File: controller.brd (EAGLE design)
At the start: 100 x 100 mm, 38 parts, among them IC1 7805DT, Q2 MOSFET-NCHANNELBSS123LT1G, Q3 MOSFET-NCHANNELFDD8780, U1 ATMEGA328P, Y1 16MHz

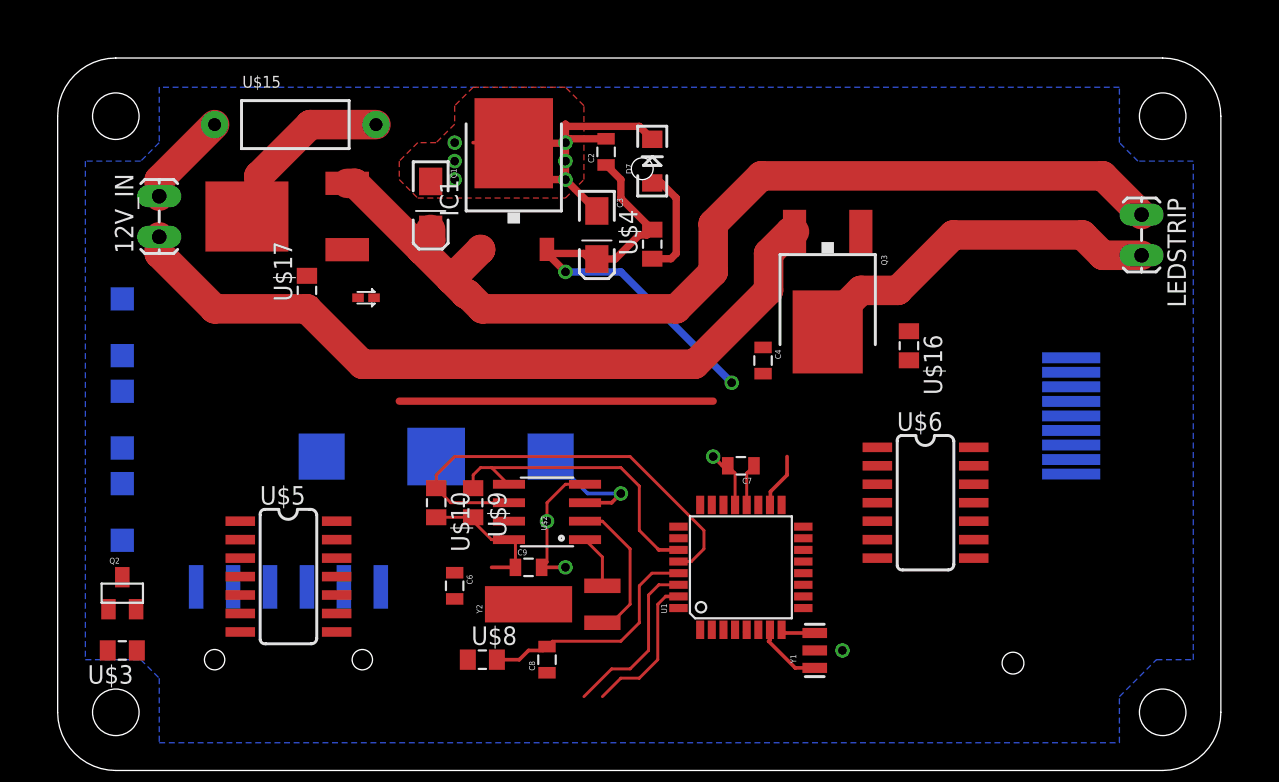
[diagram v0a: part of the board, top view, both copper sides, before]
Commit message: added sense IC footprint and jumper. layed out "high" power section.
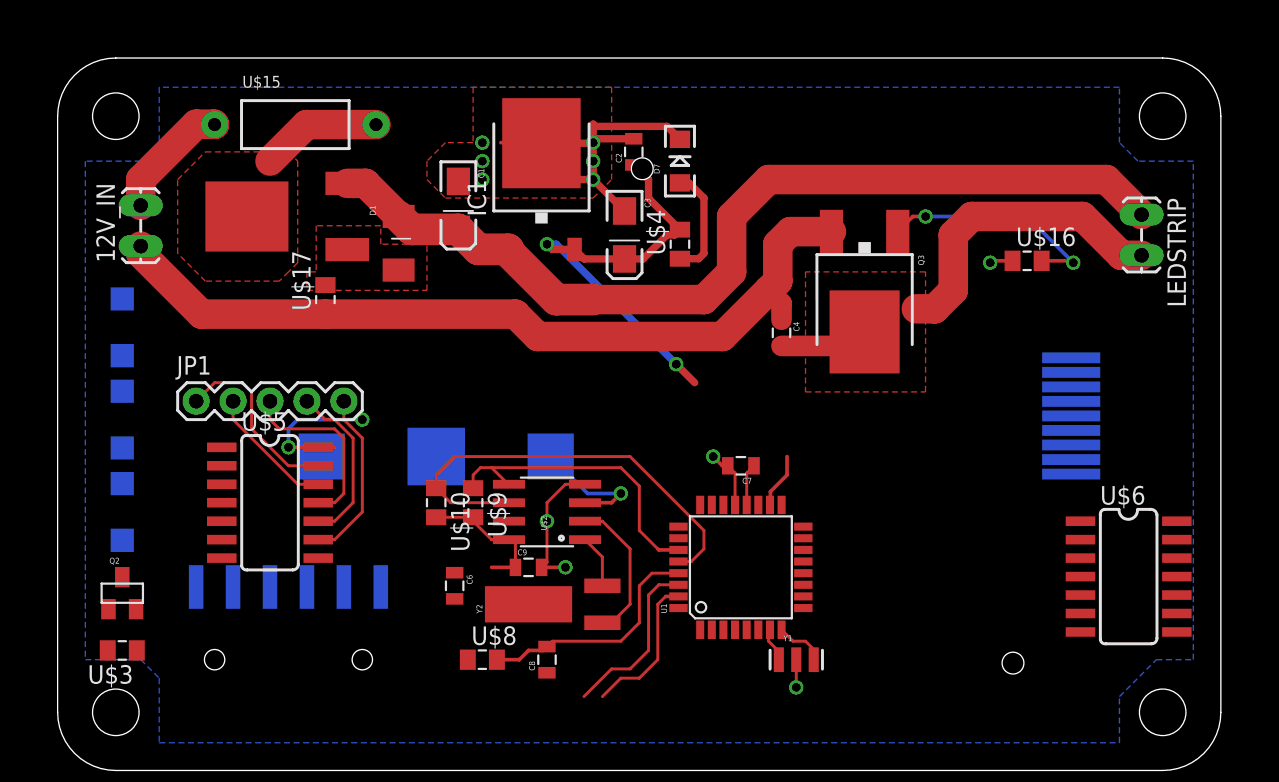
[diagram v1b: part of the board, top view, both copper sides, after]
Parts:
- added JP1: (no value), SparkFun-Connectors:1X05
- D1: device SparkFun-DiscreteSemi:SOD-523 -> jt_parts:DO-214AA
- moved U$6 14.9 mm to (78.1, 17.8)
- moved U$16 10.0 mm to (71.1, 38.9), turned to 0 degrees
- moved U$5 5.24 mm to (19.1, 22.9)
- moved D1 4.73 mm to (28.1, 40.4), turned to 270 degrees
- moved Q3 2.54 mm to (59.9, 35.6)
- moved C4 2.29 mm to (54.2, 33.9)
- moved C2 1.91 mm to (44.1, 46.4)
- moved D7 1.91 mm to (47.2, 45.7)
- moved IC1 1.91 mm to (37.7, 44.5)
- moved U$4 1.91 mm to (47.2, 40.0)
- moved C1 1.90 mm to (32.0, 42.7)
- moved C3 1.90 mm to (43.4, 40.6)
- moved Y1 1.42 mm to (55.2, 11.4), turned to 0 degrees
- moved 12V_IN 1.42 mm to (10.2, 40.0)
- moved U$17 1.42 mm to (22.9, 36.2)
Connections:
- new net KEY4: JP1.5, U$5.9
- new net N$24: JP1.4, U$5.10
- new net N$25: JP1.3, U$5.11
- new net N$26: JP1.2, U$5.12
- new net N$27: JP1.1, U$5.13
- new net OUT1: U$5.8, U1.32
- new net OUT2: U$5.7, U1.1
- new net OUT3: U$5.6
- new net OUT4: U$5.5
- net 5V: now also U$5.14
- net GND: now also U$5.1
- net VDD: now also U$6.1; no longer U$5.13, U$6.13
- net VSS: no longer U$5.14
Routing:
- net PWM_LED: track 0.00 -> 16.0 mm, vias 0 -> 2
- net N$27: track 0.00 -> 13.3 mm
- net N$25: track 0.00 -> 12.7 mm
- net KEY4: track 0.00 -> 12.0 mm
- net 5V: track 65.6 -> 53.7 mm, vias 2 -> 4
- net N$24: track 0.00 -> 11.6 mm
- net N$26: track 0.00 -> 8.97 mm
- net GND: track 93.9 -> 100.8 mm, vias 10 -> 11
- net N$14: track 25.3 -> 30.5 mm
- net N$13: track 12.6 -> 8.33 mm
- net 12V: track 69.6 -> 66.0 mm
- net N$1: track 4.76 -> 2.39 mm
- net N$8: track 6.50 -> 8.45 mm
- net N$4: track 2.37 -> 3.48 mm
- added copper zone on layer 1, net N$13
- added copper zone on layer 1, net N$14
- added copper zone on layer 1, net N$16

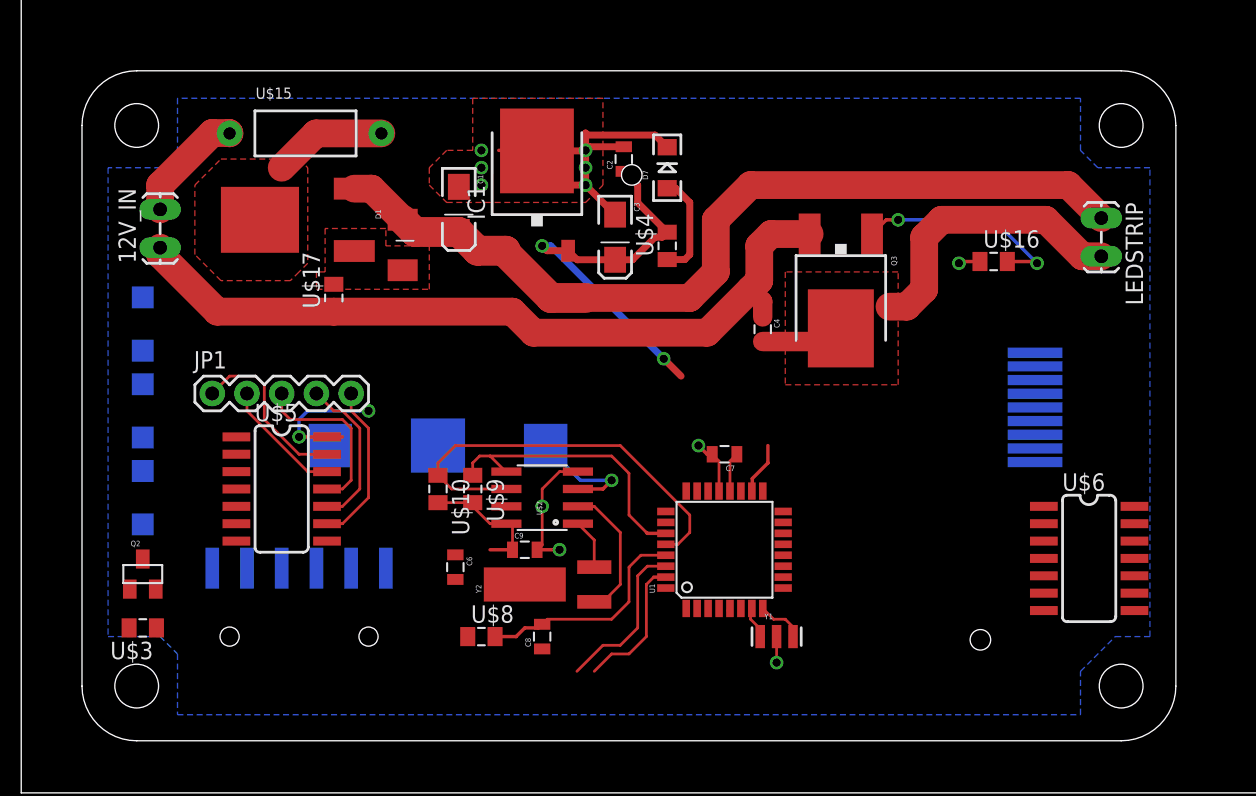
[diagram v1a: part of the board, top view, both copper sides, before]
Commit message: made 12V traces narrower. modified nokia5110 package.
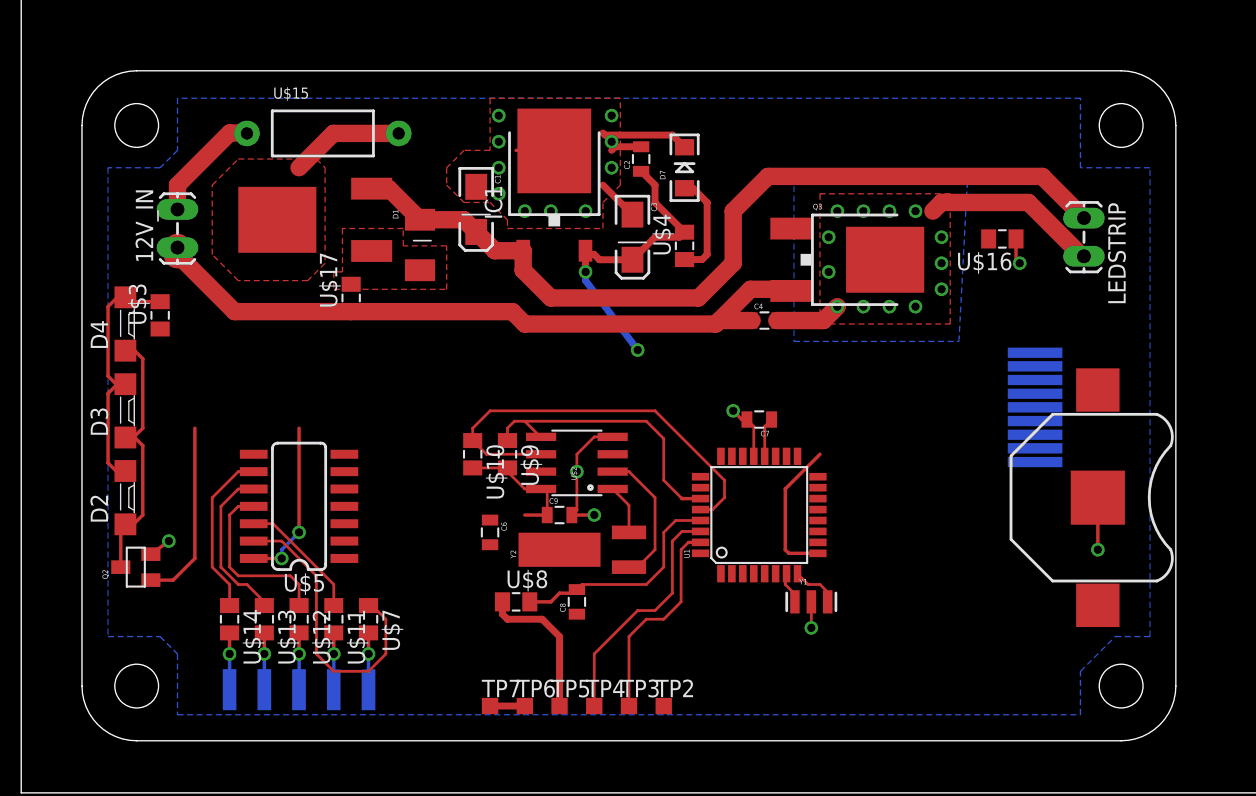
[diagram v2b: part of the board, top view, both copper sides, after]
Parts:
- removed ICP: (no value), SparkFun-Connectors:1X06-SMD
- removed JP1: (no value), SparkFun-Connectors:1X05
- removed U$6: AT42QT1070, jt_parts:SOIC-14
- added TP2, TP3, TP4, TP5, TP6, TP7: TPTP12SQ, testpad:TP12SQ
- added U$11, U$12, U$13, U$14, U$7: 10k, jt_parts:RESISTOR-0805
- added U$19: M05, jt_parts:M05-SMD
- NOKIA5110: device lph-7366:LPH-7366 -> jt_parts:NOKIA5110
- moved BAT1 48.4 mm to (78.7, 21.6), flipped to the top, turned to 270 degrees
- moved U$3 22.9 mm to (10.2, 34.9), turned to 90 degrees
- moved Q3 3.81 mm to (61.6, 39.0), turned to 270 degrees
- moved Y2 3.59 mm to (44.5, 17.8)
- moved U$10 3.59 mm to (33.0, 24.8)
- moved C8 3.59 mm to (40.6, 14.0)
- moved U$8 3.59 mm to (36.2, 14.0)
- moved Y1 3.59 mm to (57.8, 14.0)
- moved C6 3.59 mm to (34.3, 19.1)
- moved C7 3.59 mm to (54.0, 27.3)
- moved C9 3.59 mm to (39.4, 20.3)
- moved U$2 3.59 mm to (40.6, 24.1)
- moved U$9 3.59 mm to (35.6, 24.8)
- moved U1 3.59 mm to (54.0, 20.3)
- moved U$5 2.84 mm to (20.3, 20.3), turned to 90 degrees
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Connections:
- removed net VDD: U$6.1
- removed net VSS: U$6.14
- new net N$21: U$14.2, U$19.5
- new net N$28: U$13.2, U$19.4
- new net N$29: U$12.2, U$19.3
- new net N$30: U$11.2, U$19.2
- new net N$31: U$19.1, U$7.2
- net 5V: now also TP5.TP; no longer ICP.4
- net DTR: now also TP2.TP; no longer ICP.1
- net GND: now also TP6.TP, TP7.TP; no longer ICP.5, ICP.6
- net KEY4: now also U$14.1; no longer JP1.5
- net N$24: now also U$13.1; no longer JP1.4
- net N$25: now also U$12.1; no longer JP1.3
- net N$26: now also U$11.1; no longer JP1.2
- net N$27: now also U$7.1; no longer JP1.1
- net RXI: now also TP4.TP; no longer ICP.3
- net TXO: now also TP3.TP; no longer ICP.2
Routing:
- net N$12: track 0.00 -> 20.4 mm
- net N$9: track 0.00 -> 19.3 mm
- net LIGHT: track 0.00 -> 13.4 mm
- net N$14: track 30.5 -> 17.8 mm, vias 0 -> 13
- net N$27: track 13.3 -> 22.5 mm
- net VBATT: track 8.60 -> 0.00 mm, vias 1 -> 0
- net RXI: track 11.9 -> 17.5 mm
- net PWM_LED: track 16.0 -> 10.5 mm, vias 2 -> 0
- net TXO: track 10.3 -> 15.4 mm
- net GND: track 100.8 -> 95.8 mm, vias 11 -> 17
- net N$31: track 0.00 -> 4.16 mm, vias 0 -> 1
- net N$30: track 0.00 -> 4.16 mm, vias 0 -> 1
- net N$29: track 0.00 -> 4.16 mm, vias 0 -> 1
- net N$28: track 0.00 -> 4.16 mm, vias 0 -> 1
- net N$21: track 0.00 -> 4.16 mm, vias 0 -> 1
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- added copper zone on layer 16, net N$14

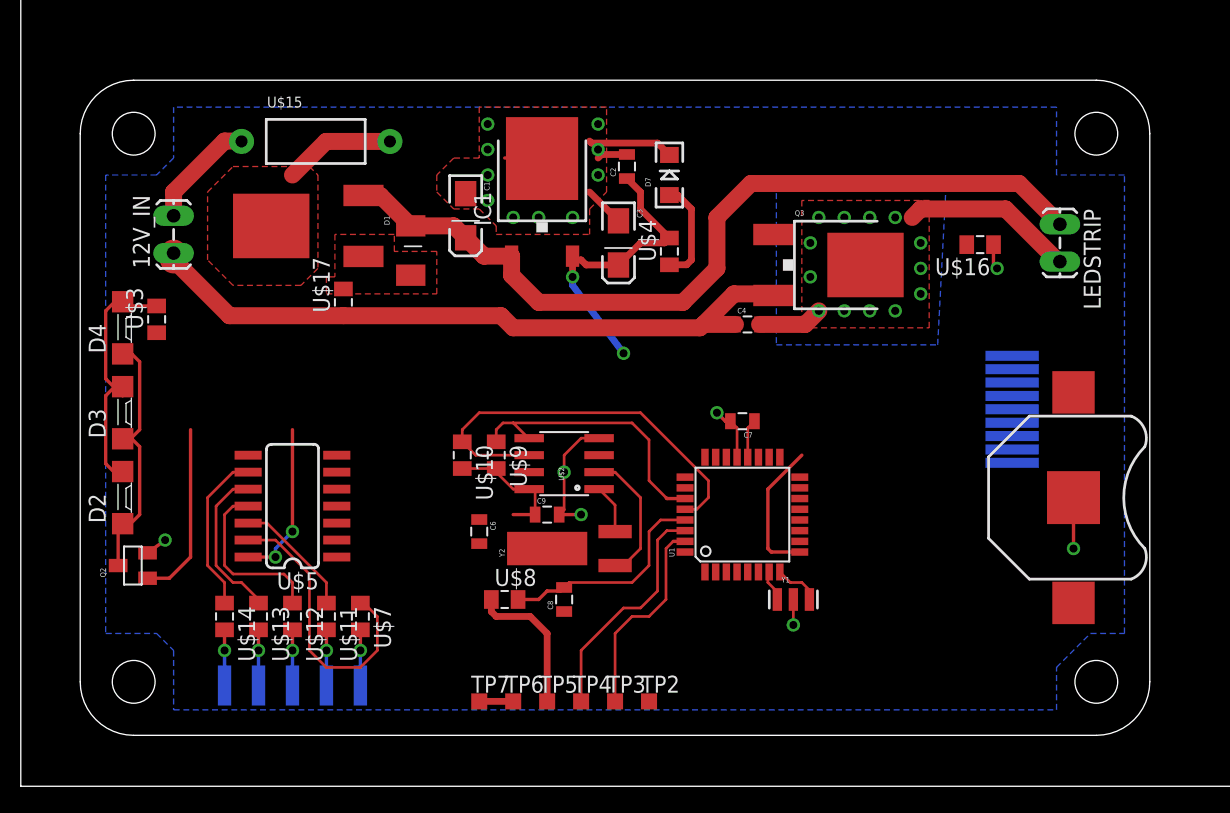
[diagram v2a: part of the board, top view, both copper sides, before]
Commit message: decreased board size
add backlight leds. changed to locking through hole programming header.
reorganized and tightened voltage regulator section.
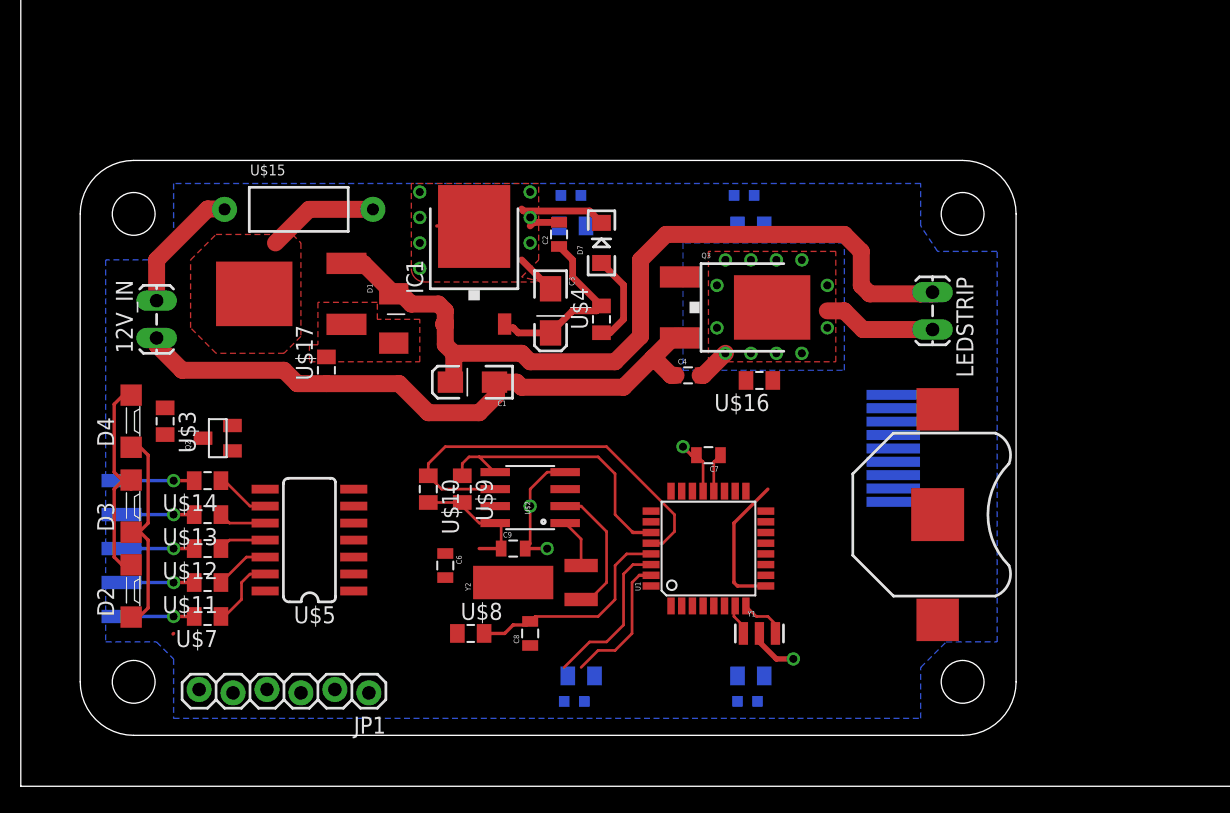
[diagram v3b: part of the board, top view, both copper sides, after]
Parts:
- removed TP2, TP3, TP4, TP5, TP6, TP7: TPTP12SQ, testpad:TP12SQ
- added JP1: (no value), SparkFun-Connectors:1X06_LOCK
- added LED1, LED2, LED3, LED4: (no value), SparkFun-LED:LED-0603
- added U$20: (no value), dp_pcb:DP7043_V1
- added U$21, U$22, U$6: 10k, jt_parts:RESISTOR-0805
- U$18: value (none) -> 10k; device dp_pcb:DP8049_V1 -> jt_parts:RESISTOR-0805
- moved U$18 53.0 mm to (41.3, 41.9), flipped to the bottom
- moved U$16 19.4 mm to (55.2, 30.4)
- moved U$19 16.3 mm to (7.62, 17.8), turned to 90 degrees
- moved C1 12.5 mm to (33.8, 30.2), turned to 180 degrees
- moved Q2 11.4 mm to (14.7, 26.0)
- moved U$7 11.4 mm to (14.0, 12.7), turned to 180 degrees
- moved LEDSTRIP 10.8 mm to (68.2, 36.8)
- moved U$14 10.2 mm to (14.0, 22.9), turned to 180 degrees
- moved BAT1 10.2 mm to (68.6, 20.3)
- moved NOKIA5110 9.36 mm to (48.3, 25.3)
- moved U$11 9.25 mm to (14.0, 15.2), turned to 180 degrees
- moved U$13 8.52 mm to (14.0, 20.3), turned to 180 degrees
- moved U$12 8.13 mm to (14.0, 17.8), turned to 180 degrees
- moved Q3 7.67 mm to (54.6, 35.8)
- moved U$3 7.65 mm to (10.8, 27.3), turned to 270 degrees
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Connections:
- removed net SQW: U$2.7
- new net N$33: LED3.A, U$18.2
- new net N$34: LED2.A, U$21.2
- new net N$35: LED1.A, U$22.2
- new net N$39: U$18.1, U$21.1, U$22.1, U$6.1
- new net OUT0: U$5.3
- net 5V: now also JP1.4; no longer TP5.TP
- net DTR: now also JP1.1; no longer TP2.TP
- net GND: now also JP1.5, JP1.6, LED1.C, LED2.C, LED3.C, LED4.C; no longer TP6.TP, TP7.TP
- net N$22: now also LED4.A, U$6.2; no longer NOKIA5110.8
- net RXI: now also JP1.3; no longer TP4.TP
- net TXO: now also JP1.2; no longer TP3.TP
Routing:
- net 5V: track 55.4 -> 23.9 mm, vias 4 -> 0
- net N$27: track 22.5 -> 5.36 mm
- net LIGHT: track 13.4 -> 0.00 mm
- net GND: track 95.8 -> 85.2 mm, vias 17 -> 11
- net N$25: track 13.0 -> 3.57 mm
- net N$24: track 11.9 -> 3.57 mm
- net KEY4: track 12.2 -> 4.09 mm
- net N$14: track 17.8 -> 11.0 mm, vias 13 -> 12
- net RXI: track 17.5 -> 11.9 mm
- net N$26: track 9.24 -> 4.09 mm
- net TXO: track 15.4 -> 10.3 mm
- net N$12: track 20.4 -> 17.8 mm
- net N$9: track 19.3 -> 17.0 mm
- net N$31: track 4.16 -> 5.43 mm
- net N$30: track 4.16 -> 5.43 mm
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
